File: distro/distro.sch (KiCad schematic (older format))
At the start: 26 parts, among them K1 CONN_3, P1 CONN_2, P10 CONN_2, P11 CONN_2, P12 CONN_2, P2 CONN_2, P3 CONN_2, P4 CONN_2, P5 CONN_2, P6 CONN_2, P7 CONN_2, P8 CONN_2, P9 CONN_2, U1 KBVW006A0B

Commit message: started on t/r with enclosure, migrated distro to 15v
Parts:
- removed C10, C6: 1000 pF, symbol C
- removed C11, C8: 1 uF, symbol C
- removed C7: 22 nF, symbol C
- removed C9: 10 uF, symbol C
- removed U1: KBVW006A0B, symbol KBVW006A0B
- added P13: CONN_2, local:0015311026, symbol CONN_2
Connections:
- wire segments 83 -> 67
- no-connect marks 3 -> 1
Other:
- note added: "12V AUX"
- note added: "12V input"
- note removed: "12V AUX input"
- note removed: "KBVW006A0B DC/DC converter"
- note removed: "positive logic, default pin length\n"

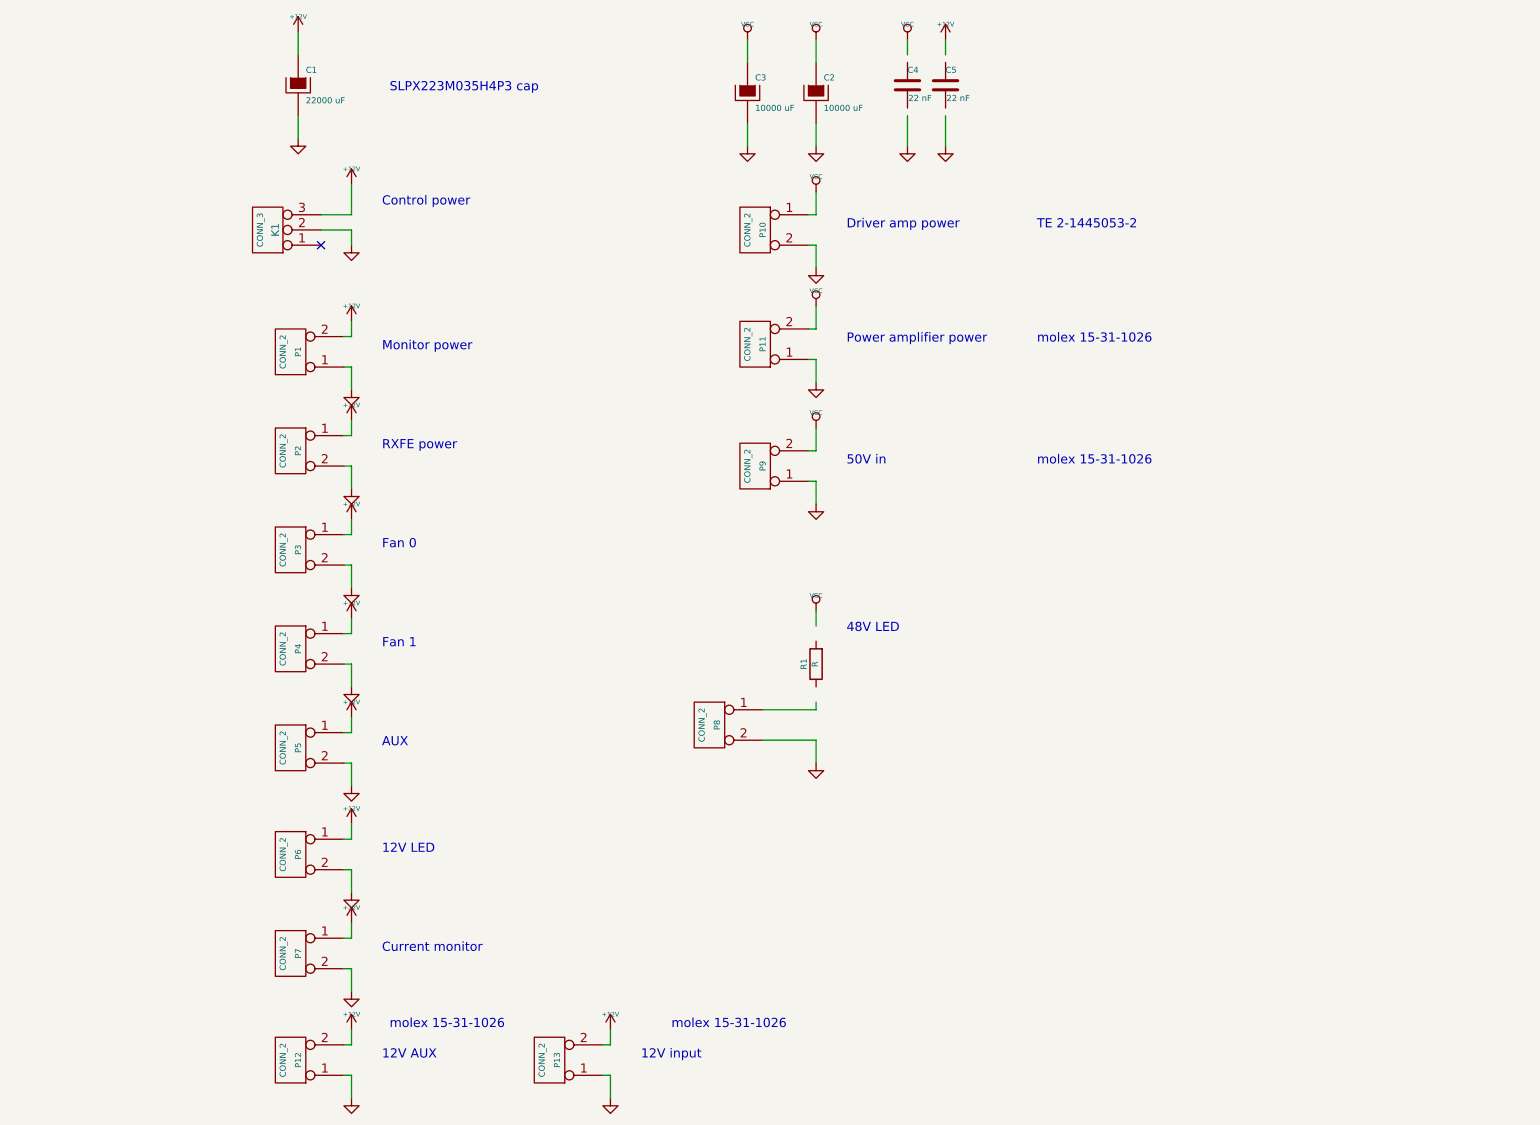
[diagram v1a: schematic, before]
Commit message: added fiducial marker footprint and marks to control board. increased default solderpaste clearance to .05 mm on control
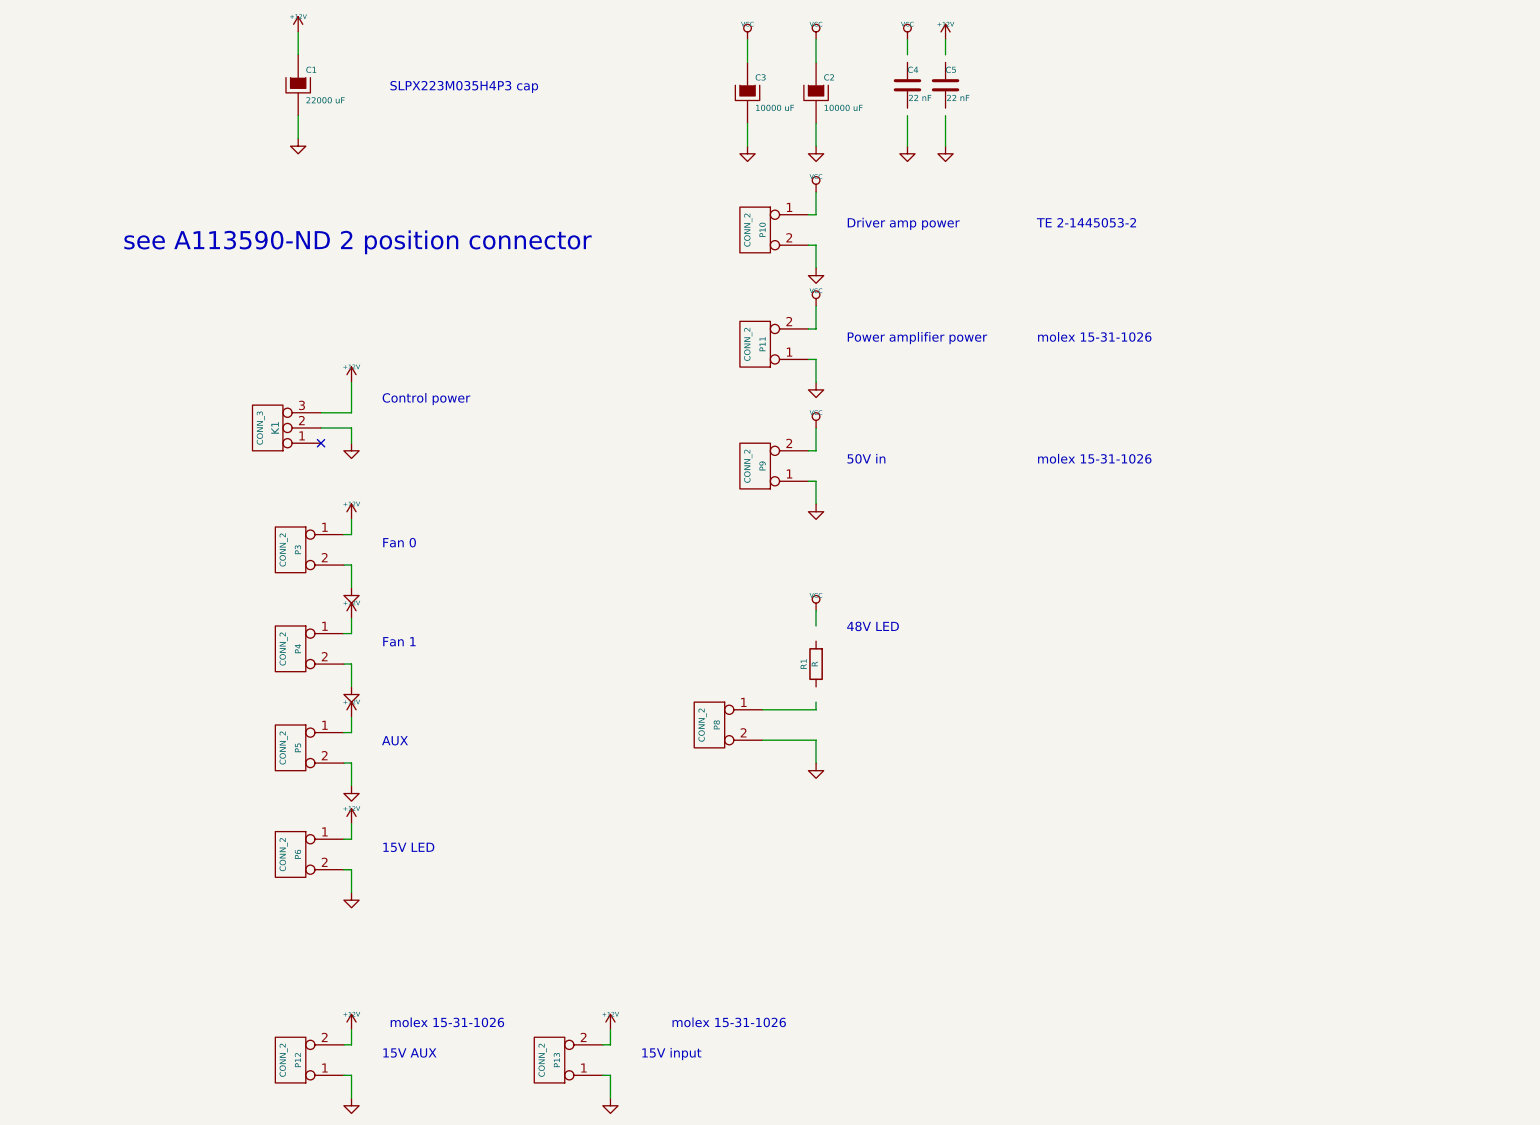
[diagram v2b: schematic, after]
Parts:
- removed P1: CONN_2, local:0015311026, symbol CONN_2
- removed P2, P7: CONN_2, Connect:PINHEAD1-2, symbol CONN_2
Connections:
- wire segments 67 -> 55
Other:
- note added: "15V AUX"
- note added: "15V LED"
- note added: "15V input"
- note added: "see A113590-ND 2 position connector"
- note removed: "12V AUX"
- note removed: "12V LED"
- note removed: "12V input"
- note removed: "Current monitor"
- note removed: "Monitor power\n"
- note removed: "RXFE power"
- moved on the sheet: K1
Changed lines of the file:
@@
 LIBS:valves
 LIBS:kbvw006a0b
+LIBS:distro-cache
 EELAYER 24 0
 EELAYER END
@@
 L CONN_3 K1
 U 1 1 5408CC8C
-P 2500 1950
-F 0 "K1" V 2450 1950 50  0000 C CNN
-F 1 "CONN_3" V 2550 1950 40  0000 C CNN
-F 2 "Connect:PINHEAD1-3" H 2500 1950 60  0001 C CNN
-F 3 "" H 2500 1950 60  0000 C CNN
-	1    2500 1950
+P 2500 3250
+F 0 "K1" V 2450 3250 50  0000 C CNN
+F 1 "CONN_3" V 2550 3250 40  0000 C CNN
+F 2 "Connect:PINHEAD1-3" H 2500 3250 60  0001 C CNN
+F 3 "" H 2500 3250 60  0000 C CNN
+	1    2500 3250
 	-1   0    0    1
-$EndComp
-$Comp
-L +12V #PWR7
-U 1 1 5408CCA0
-P 3050 3200
-F 0 "#PWR7" H 3050 3150 20  0001 C CNN
-F 1 "+12V" H 3050 3300 30  0000 C CNN
-F 2 "" H 3050 3200 60  0000 C CNN
-F 3 "" H 3050 3200 60  0000 C CNN
-	1    3050 3200
-	1    0    0    -1
 $EndComp
 $Comp
@@
 F 3 "" H 6100 700 60  0000 C CNN
 	1    6100 700
-	1    0    0    -1
-$EndComp
-$Comp
-L CONN_2 P2
-U 1 1 5408CD5B
-P 2650 3400
-F 0 "P2" V 2600 3400 40  0000 C CNN
-F 1 "CONN_2" V 2700 3400 40  0000 C CNN
-F 2 "Connect:PINHEAD1-2" H 2650 3400 60  0001 C CNN
-F 3 "" H 2650 3400 60  0000 C CNN
-	1    2650 3400
-	-1   0    0    -1
-$EndComp
-$Comp
-L GND #PWR8
-U 1 1 5408CD81
-P 3050 3650
-F 0 "#PWR8" H 3050 3650 30  0001 C CNN
-F 1 "GND" H 3050 3580 30  0001 C CNN
-F 2 "" H 3050 3650 60  0000 C CNN
-F 3 "" H 3050 3650 60  0000 C CNN
-	1    3050 3650
 	1    0    0    -1
 $EndComp
@@
 	1    0    0    -1
 $EndComp
-Text Notes 3250 3400 0    60   ~ 0
-RXFE power
 Text Notes 3250 4050 0    60   ~ 0
 Fan 0
@@
 AUX
 $Comp
-L +12V #PWR5
-U 1 1 5408CE2B
-P 3050 2550
-F 0 "#PWR5" H 3050 2500 20  0001 C CNN
-F 1 "+12V" H 3050 2650 30  0000 C CNN
-F 2 "" H 3050 2550 60  0000 C CNN
-F 3 "" H 3050 2550 60  0000 C CNN
-	1    3050 2550
-	1    0    0    -1
-$EndComp
-$Comp
-L CONN_2 P1
-U 1 1 5408CE31
-P 2650 2750
-F 0 "P1" V 2600 2750 40  0000 C CNN
-F 1 "CONN_2" V 2700 2750 40  0000 C CNN
-F 2 "local:0015311026" H 2650 2750 60  0001 C CNN
-F 3 "" H 2650 2750 60  0000 C CNN
-	1    2650 2750
-	-1   0    0    1
-$EndComp
-$Comp
-L GND #PWR6
-U 1 1 5408CE37
-P 3050 3000
-F 0 "#PWR6" H 3050 3000 30  0001 C CNN
-F 1 "GND" H 3050 2930 30  0001 C CNN
-F 2 "" H 3050 3000 60  0000 C CNN
-F 3 "" H 3050 3000 60  0000 C CNN
-	1    3050 3000
-	1    0    0    -1
-$EndComp
-Text Notes 3250 2750 0    60   ~ 0
-Monitor power\n
-$Comp
 L +12V #PWR15
 U 1 1 5408CE68
@@
 $EndComp
 Text Notes 3250 6050 0    60   ~ 0
-12V LED
-$Comp
-L +12V #PWR17
-U 1 1 5408CE80
-P 3050 6500
-F 0 "#PWR17" H 3050 6450 20  0001 C CNN
-F 1 "+12V" H 3050 6600 30  0000 C CNN
-F 2 "" H 3050 6500 60  0000 C CNN
-F 3 "" H 3050 6500 60  0000 C CNN
-	1    3050 6500
-	1    0    0    -1
-$EndComp
-$Comp
-L CONN_2 P7
-U 1 1 5408CE86
-P 2650 6700
-F 0 "P7" V 2600 6700 40  0000 C CNN
-F 1 "CONN_2" V 2700 6700 40  0000 C CNN
-F 2 "Connect:PINHEAD1-2" H 2650 6700 60  0001 C CNN
-F 3 "" H 2650 6700 60  0000 C CNN
-	1    2650 6700
-	-1   0    0    -1
-$EndComp
-$Comp
-L GND #PWR18
-U 1 1 5408CE8C
-P 3050 6950
-F 0 "#PWR18" H 3050 6950 30  0001 C CNN
-F 1 "GND" H 3050 6880 30  0001 C CNN
-F 2 "" H 3050 6950 60  0000 C CNN
-F 3 "" H 3050 6950 60  0000 C CNN
-	1    3050 6950
-	1    0    0    -1
-$EndComp
-Text Notes 3250 6700 0    60   ~ 0
-Current monitor
+15V LED
 $Comp
 L CONN_2 P11
@@
 L GND #PWR4
 U 1 1 5408CFEC
-P 3050 2050
-F 0 "#PWR4" H 3050 2050 30  0001 C CNN
-F 1 "GND" H 3050 1980 30  0001 C CNN
-F 2 "" H 3050 2050 60  0000 C CNN
-F 3 "" H 3050 2050 60  0000 C CNN
-	1    3050 2050
-	1    0    0    -1
-$EndComp
-NoConn ~ 2850 2050
+P 3050 3350
+F 0 "#PWR4" H 3050 3350 30  0001 C CNN
+F 1 "GND" H 3050 3280 30  0001 C CNN
+F 2 "" H 3050 3350 60  0000 C CNN
+F 3 "" H 3050 3350 60  0000 C CNN
+	1    3050 3350
+	1    0    0    -1
+$EndComp
+NoConn ~ 2850 3350
 $Comp
 L +12V #PWR3
 U 1 1 5408D027
-P 3050 1650
-F 0 "#PWR3" H 3050 1600 20  0001 C CNN
-F 1 "+12V" H 3050 1750 30  0000 C CNN
-F 2 "" H 3050 1650 60  0000 C CNN
-F 3 "" H 3050 1650 60  0000 C CNN
-	1    3050 1650
-	1    0    0    -1
-$EndComp
-Text Notes 3250 1800 0    60   ~ 0
+P 3050 2950
+F 0 "#PWR3" H 3050 2900 20  0001 C CNN
+F 1 "+12V" H 3050 3050 30  0000 C CNN
+F 2 "" H 3050 2950 60  0000 C CNN
+F 3 "" H 3050 2950 60  0000 C CNN
+	1    3050 2950
+	1    0    0    -1
+$EndComp
+Text Notes 3250 3100 0    60   ~ 0
 Control power
 $Comp
@@
 $EndComp
 Text Notes 3250 7400 0    60   ~ 0
-12V AUX
-Wire Wire Line
-	2700 1350 2700 1200
-Wire Wire Line
-	2700 650  2700 800
-Wire Wire Line
-	6100 1400 6100 1250
-Wire Wire Line
-	6100 700  6100 850
-Wire Wire Line
-	3000 3300 3050 3300
-Wire Wire Line
-	3050 3300 3050 3200
-Wire Wire Line
-	3000 3500 3050 3500
-Wire Wire Line
-	3050 3500 3050 3650
-Wire Wire Line
-	3000 3950 3050 3950
-Wire Wire Line
-	3050 3950 3050 3850
-Wire Wire Line
-	3000 4150 3050 4150
-Wire Wire Line
-	3050 4150 3050 4300
-Wire Wire Line
-	3000 4600 3050 4600
-Wire Wire Line
-	3050 4600 3050 4500
-Wire Wire Line
-	3000 4800 3050 4800
-Wire Wire Line
-	3050 4800 3050 4950
-Wire Wire Line
-	3000 5250 3050 5250
-Wire Wire Line
-	3050 5250 3050 5150
-Wire Wire Line
-	3000 5450 3050 5450
-Wire Wire Line
-	3050 5450 3050 5600
-Wire Wire Line
-	3000 2650 3050 2650
-Wire Wire Line
-	3050 2650 3050 2550
-Wire Wire Line
-	3000 2850 3050 2850
-Wire Wire Line
-	3050 2850 3050 3000
-Wire Wire Line
-	3000 5950 3050 5950
-Wire Wire Line
-	3050 5950 3050 5850
-Wire Wire Line
-	3000 6150 3050 6150
-Wire Wire Line
-	3050 6150 3050 6300
-Wire Wire Line
-	3000 6600 3050 6600
-Wire Wire Line
-	3050 6600 3050 6500
-Wire Wire Line
-	3000 6800 3050 6800
-Wire Wire Line
-	3050 6800 3050 6950
-Wire Wire Line
-	6100 2600 6050 2600
-Wire Wire Line
-	6100 2450 6100 2600
-Wire Wire Line
-	6050 2800 6100 2800
-Wire Wire Line
-	6100 2800 6100 2950
-Wire Wire Line
-	6100 1850 6050 1850
-Wire Wire Line
-	6100 1700 6100 1850
-Wire Wire Line
-	6050 2050 6100 2050
-Wire Wire Line
-	6100 2050 6100 2200
-Wire Wire Line
-	5750 5300 6100 5300
-Wire Wire Line
-	6100 5300 6100 5450
-Wire Wire Line
-	2850 1950 3050 1950
-Wire Wire Line
-	3050 1950 3050 2050
-Wire Wire Line
-	3050 1650 3050 1850
-Wire Wire Line
-	3050 1850 2850 1850
-Wire Wire Line
-	6100 4450 6100 4550
-Wire Wire Line
-	5750 5100 6100 5100
-Wire Wire Line
-	6100 5100 6100 5050
-Wire Wire Line
-	6100 3400 6050 3400
-Wire Wire Line
-	6100 3250 6100 3400
-Wire Wire Line
-	6050 3600 6100 3600
-Wire Wire Line
-	6100 3600 6100 3750
-Wire Wire Line
-	5650 1400 5650 1250
-Wire Wire Line
-	5650 700  5650 850
-Wire Wire Line
-	6950 700  6950 800
-Wire Wire Line
-	6700 700  6700 800
-Wire Wire Line
-	6700 1200 6700 1400
-Wire Wire Line
-	6950 1200 6950 1400
-Wire Wire Line
-	3000 7300 3050 7300
-Wire Wire Line
-	3050 7300 3050 7200
-Wire Wire Line
-	3000 7500 3050 7500
-Wire Wire Line
-	3050 7500 3050 7650
+15V AUX
 $Comp
 L +12V #PWR21
@@
 $EndComp
 Text Notes 4950 7400 0    60   ~ 0
-12V input
-Wire Wire Line
-	4700 7300 4750 7300
-Wire Wire Line
-	4750 7300 4750 7200
-Wire Wire Line
-	4700 7500 4750 7500
-Wire Wire Line
-	4750 7500 4750 7650
+15V input
 Text Notes 5150 7200 0    60   ~ 0
 molex 15-31-1026
 Text Notes 3300 7200 0    60   ~ 0
 molex 15-31-1026
+Wire Wire Line
+	2700 1350 2700 1200
+Wire Wire Line
+	2700 650  2700 800
+Wire Wire Line
+	6100 1400 6100 1250
+Wire Wire Line
+	6100 700  6100 850
+Wire Wire Line
+	3000 3950 3050 3950
+Wire Wire Line
+	3050 3950 3050 3850
+Wire Wire Line
+	3000 4150 3050 4150
+Wire Wire Line
+	3050 4150 3050 4300
+Wire Wire Line
+	3000 4600 3050 4600
+Wire Wire Line
+	3050 4600 3050 4500
+Wire Wire Line
+	3000 4800 3050 4800
+Wire Wire Line
+	3050 4800 3050 4950
+Wire Wire Line
+	3000 5250 3050 5250
+Wire Wire Line
+	3050 5250 3050 5150
+Wire Wire Line
+	3000 5450 3050 5450
+Wire Wire Line
+	3050 5450 3050 5600
+Wire Wire Line
+	3000 5950 3050 5950
+Wire Wire Line
+	3050 5950 3050 5850
+Wire Wire Line
+	3000 6150 3050 6150
+Wire Wire Line
+	3050 6150 3050 6300
+Wire Wire Line
+	6100 2600 6050 2600
+Wire Wire Line
+	6100 2450 6100 2600
+Wire Wire Line
+	6050 2800 6100 2800
+Wire Wire Line
+	6100 2800 6100 2950
+Wire Wire Line
+	6100 1850 6050 1850
+Wire Wire Line
+	6100 1700 6100 1850
+Wire Wire Line
+	6050 2050 6100 2050
+Wire Wire Line
+	6100 2050 6100 2200
+Wire Wire Line
+	5750 5300 6100 5300
+Wire Wire Line
+	6100 5300 6100 5450
+Wire Wire Line
+	2850 3250 3050 3250
+Wire Wire Line
+	3050 3250 3050 3350
+Wire Wire Line
+	3050 2950 3050 3150
+Wire Wire Line
+	3050 3150 2850 3150
+Wire Wire Line
+	6100 4450 6100 4550
+Wire Wire Line
+	5750 5100 6100 5100
+Wire Wire Line
+	6100 5100 6100 5050
+Wire Wire Line
+	6100 3400 6050 3400
+Wire Wire Line
+	6100 3250 6100 3400
+Wire Wire Line
+	6050 3600 6100 3600
+Wire Wire Line
+	6100 3600 6100 3750
+Wire Wire Line
+	5650 1400 5650 1250
+Wire Wire Line
+	5650 700  5650 850
+Wire Wire Line
+	6950 700  6950 800
+Wire Wire Line
+	6700 700  6700 800
+Wire Wire Line
+	6700 1200 6700 1400
+Wire Wire Line
+	6950 1200 6950 1400
+Wire Wire Line
+	3000 7300 3050 7300
+Wire Wire Line
+	3050 7300 3050 7200
+Wire Wire Line
+	3000 7500 3050 7500
+Wire Wire Line
+	3050 7500 3050 7650
+Wire Wire Line
+	4700 7300 4750 7300
+Wire Wire Line
+	4750 7300 4750 7200
+Wire Wire Line
+	4700 7500 4750 7500
+Wire Wire Line
+	4750 7500 4750 7650
+Text Notes 1550 2100 0    118  ~ 0
+see A113590-ND 2 position connector
 $EndSCHEMATC
